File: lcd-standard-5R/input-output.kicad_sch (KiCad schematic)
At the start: 20 parts, among them J8 Serial, J9 Conn_01x10_MountingPin, Q2 MMBT3904, Q3 MMBT3904, Q4 MMBT3904, SW3 BOOT0, SW4 RST

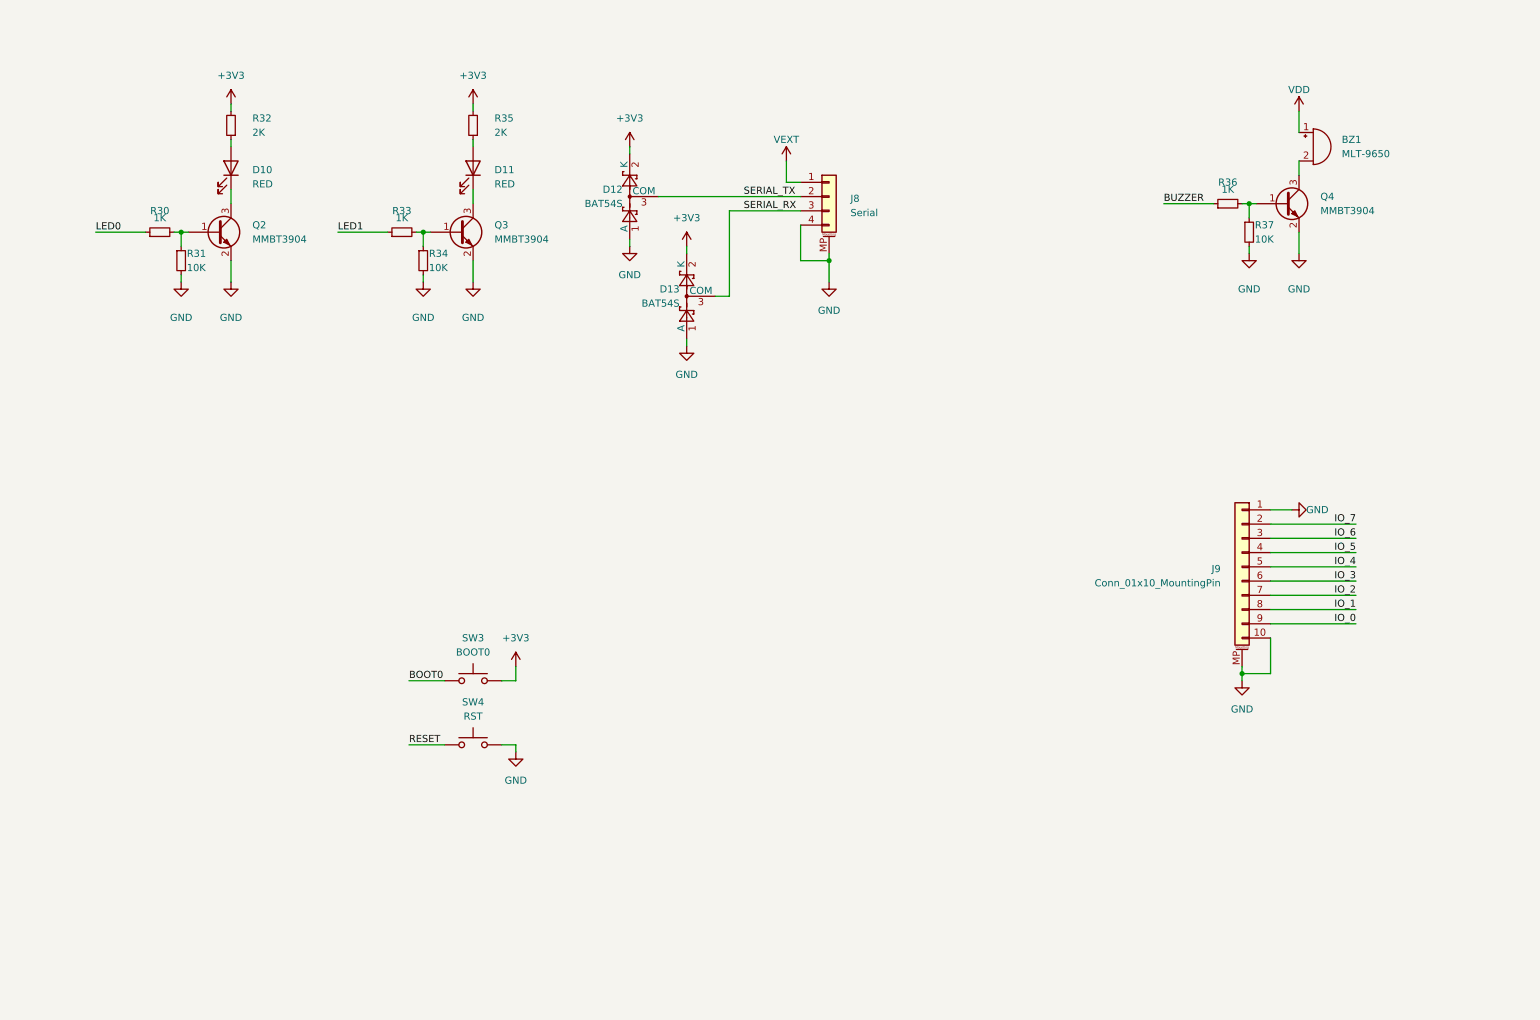
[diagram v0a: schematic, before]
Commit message: Change MCU to STM32H743
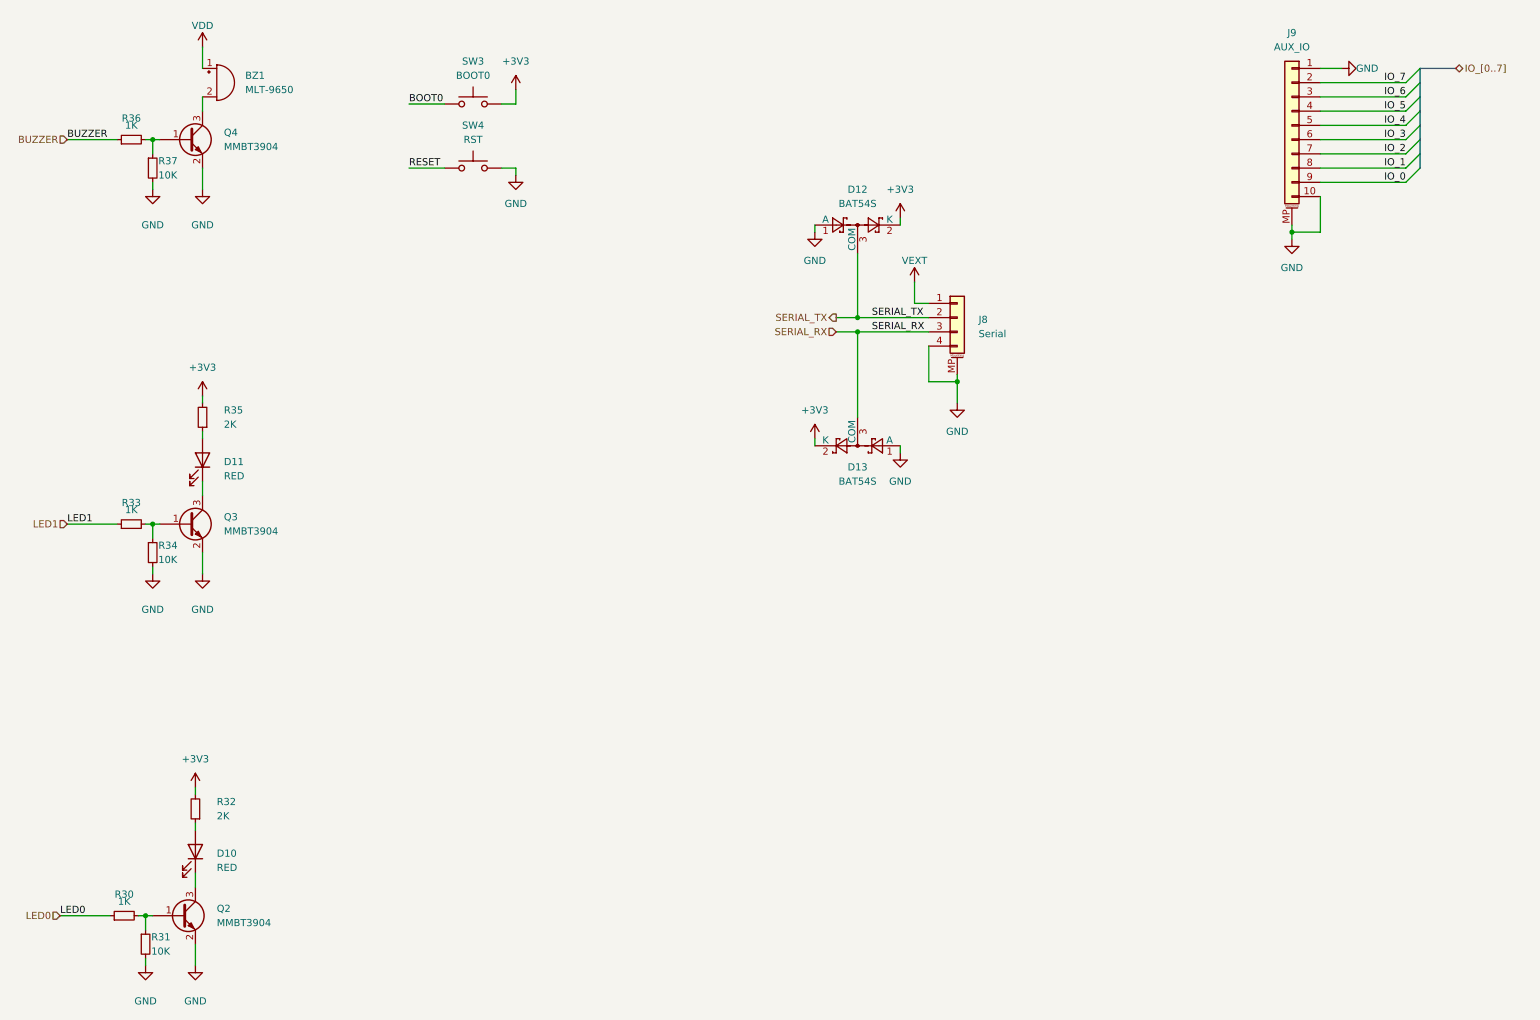
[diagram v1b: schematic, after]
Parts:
- J9: value Conn_01x10_MountingPin -> AUX_IO
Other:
- moved on the sheet: BZ1, D10, D11, D12, D13, J8, J9, Q2, Q3, Q4, R30, R31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

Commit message: Finsihed, need to touch up a bit
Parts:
- added C58, C59: 100n, Capacitor_SMD:C_0402_1005Metric, symbol Device:C_Small
- added R41, R42: 10K, Resistor_SMD:R_0402_1005Metric, symbol Device:R_Small
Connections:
- net +3V3: now also R41.1, R42.1; no longer SW3.2
- net GND: now also SW3.2, C58.2, C59.2
- net BOOT0 renamed BTN_0
- net BTN_0: now also C58.1, R41.2
- net RESET renamed BTN_1
- net BTN_1: now also C59.1, R42.2
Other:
- moved on the sheet: SW4

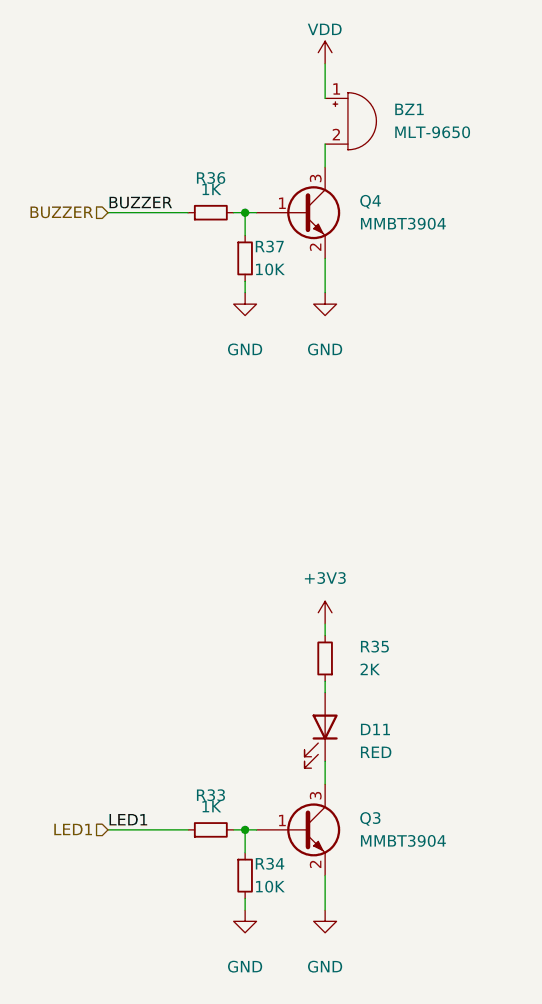
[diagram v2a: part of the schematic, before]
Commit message: Adding filter on MAX98357, TODO: Add more grounding vias
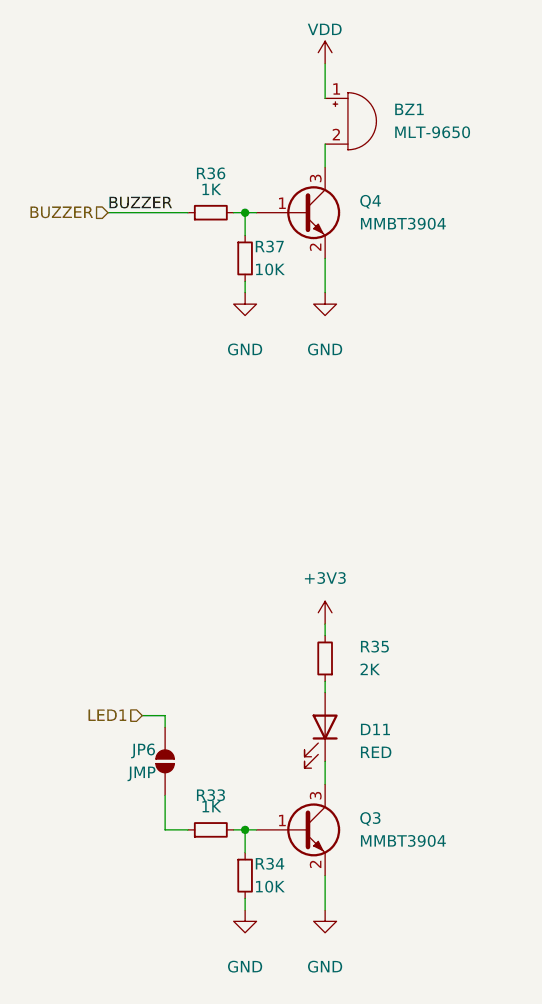
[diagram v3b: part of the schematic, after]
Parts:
- added JP6: JMP, Jumper:SolderJumper-2_P1.3mm_Open_RoundedPad1.0x1.5mm, symbol Jumper:SolderJumper_2_Open
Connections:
- net LED1: now also JP6.2 (B); no longer R33.1
- new net: JP6.1 (A), R33.1
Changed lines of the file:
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@@
 	(wire
 		(pts
+			(xy 27.94 95.25) (xy 30.48 95.25)
+		)
+		(stroke
+			(width 0)
+			(type default)
+		)
+	)
+	(wire
+		(pts
 			(xy 177.8 82.55) (xy 182.88 82.55)
 		)
@@
 	(wire
 		(pts
+			(xy 30.48 95.25) (xy 30.48 96.52)
+		)
+		(stroke
+			(width 0)
+			(type default)
+		)
+	)
+	(wire
+		(pts
 			(xy 22.86 177.8) (xy 31.75 177.8)
 		)
@@
 	(wire
 		(pts
+			(xy 30.48 107.95) (xy 33.02 107.95)
+		)
+		(stroke
+			(width 0)
+			(type default)
+		)
+	)
+	(wire
+		(pts
 			(xy 182.88 86.36) (xy 182.88 82.55)
 		)
@@
 	(wire
 		(pts
+			(xy 30.48 104.14) (xy 30.48 107.95)
+		)
+		(stroke
+			(width 0)
+			(type default)
+		)
+	)
+	(wire
+		(pts
 			(xy 242.57 55.88) (xy 242.57 54.61)
 		)
@@
 	(wire
 		(pts
-			(xy 24.13 107.95) (xy 33.02 107.95)
-		)
-		(stroke
-			(width 0)
-			(type default)
-		)
-	)
-	(wire
-		(pts
 			(xy 262.89 36.83) (xy 247.65 36.83)
 		)
@@
 		)
 	)
-	(label "LED1"
-		(at 24.13 107.95 0)
-		(fields_autoplaced yes)
-		(effects
-			(font
-				(size 1.27 1.27)
-			)
-			(justify left bottom)
-		)
-	)
 	(label "IO_7"
 		(at 262.89 29.21 180)
@@
 	(hierarchical_label "LED1"
 		(shape input)
-		(at 24.13 107.95 180)
+		(at 27.94 95.25 180)
 		(fields_autoplaced yes)
 		(effects
@@
 		(on_board yes)
 		(dnp no)
-		(fields_autoplaced yes)
 		(property "Reference" "R36"
-			(at 35.56 35.56 90)
+			(at 35.56 35.052 90)
 			(effects
 				(font
@@
 					(unit 1)
 				)
+			)
+		)
+	)
+	(symbol
+		(lib_id "Jumper:SolderJumper_2_Open")
+		(at 30.48 100.33 270)
+		(mirror x)
+		(unit 1)
+		(exclude_from_sim yes)
+		(in_bom no)
+		(on_board yes)
+		(dnp no)
+		(property "Reference" "JP6"
+			(at 29.464 99.06 90)
+			(effects
+				(font
+					(size 1.27 1.27)
+				)
+				(justify right)
+			)
+		)
+		(property "Value" "JMP"
+			(at 29.464 101.6 90)
+			(effects
+				(font
+					(size 1.27 1.27)
+				)
+				(justify right)
+			)
+		)
+		(property "Footprint" "Jumper:SolderJumper-2_P1.3mm_Open_RoundedPad1.0x1.5mm"
+			(at 30.48 100.33 0)
+			(effects
+				(font
+					(size 1.27 1.27)
+				)
+				(hide yes)
+			)
+		)
+		(property "Datasheet" "~"
+			(at 30.48 100.33 0)
+			(effects
+				(font
+					(size 1.27 1.27)
+				)
+				(hide yes)
+			)
+		)
+		(property "Description" "Solder Jumper, 2-pole, open"
+			(at 30.48 100.33 0)
+			(effects
+				(font
+					(size 1.27 1.27)
+				)
+				(hide yes)
+			)
+		)
+		(property "JLCPCB Part #" ""
+			(at 30.48 100.33 0)
+			(effects
+				(font
+					(size 1.27 1.27)
+				)
+				(hide yes)
+			)
+		)
+		(pin "1"
+		)
+		(pin "2"
+		)
+		(instances
+			(project "lcd-standard-5R"
+				(path "/a9fe5be7-3a80-455e-a721-d53819db4a52/fe784777-4ebf-46af-8dff-f54c8123e5a9"
+					(reference "JP6")
+					(unit 1)
+				)

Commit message: Add QSPI Flash trace length matching to 5 inch LCD
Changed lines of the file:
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@@
 (kicad_sch
-	(version 20231120)
+	(version 20250114)
 	(generator "eeschema")
-	(generator_version "8.0")
+	(generator_version "9.0")
 	(paper "A4")
 	(junction
@@
 	(label "IO_2"
 		(at 262.89 41.91 180)
-		(fields_autoplaced yes)
 		(effects
 			(font
@@
 	(label "LED0"
 		(at 22.86 177.8 0)
-		(fields_autoplaced yes)
 		(effects
 			(font
@@
 	(label "IO_6"
 		(at 262.89 31.75 180)
-		(fields_autoplaced yes)
 		(effects
 			(font
@@
 	(label "IO_5"
 		(at 262.89 34.29 180)
-		(fields_autoplaced yes)
 		(effects
 			(font
@@
 	(label "IO_0"
 		(at 262.89 46.99 180)
-		(fields_autoplaced yes)
 		(effects
 			(font
@@
 	(label "IO_4"
 		(at 262.89 36.83 180)
-		(fields_autoplaced yes)
 		(effects
 			(font
@@
 	(label "BUZZER"
 		(at 24.13 39.37 0)
-		(fields_autoplaced yes)
 		(effects
 			(font
@@
 	(label "IO_1"
 		(at 262.89 44.45 180)
-		(fields_autoplaced yes)
 		(effects
 			(font
@@
 	(label "SERIAL_TX"
 		(at 167.64 71.12 0)
-		(fields_autoplaced yes)
 		(effects
 			(font
@@
 	(label "IO_3"
 		(at 262.89 39.37 180)
-		(fields_autoplaced yes)
 		(effects
 			(font
@@
 	(label "IO_7"
 		(at 262.89 29.21 180)
-		(fields_autoplaced yes)
 		(effects
 			(font
@@
 	(label "SERIAL_RX"
 		(at 167.64 73.66 0)
-		(fields_autoplaced yes)
 		(effects
 			(font
@@
 		(shape input)
 		(at 161.29 73.66 180)
-		(fields_autoplaced yes)
 		(effects
 			(font
@@
 		(shape output)
 		(at 85.09 33.02 180)
-		(fields_autoplaced yes)
 		(effects
 			(font
@@
 		(shape input)
 		(at 24.13 39.37 180)
-		(fields_autoplaced yes)
 		(effects
 			(font
@@
 		(shape input)
 		(at 27.94 95.25 180)
-		(fields_autoplaced yes)
 		(effects
 			(font
@@
 		(shape bidirectional)
 		(at 271.78 26.67 0)
-		(fields_autoplaced yes)
 		(effects
 			(font
@@
 		(shape output)
 		(at 161.29 71.12 180)
-		(fields_autoplaced yes)
 		(effects
 			(font
@@
 		(shape output)
 		(at 85.09 67.31 180)
-		(fields_autoplaced yes)
 		(effects
 			(font
@@
 		(shape input)
 		(at 22.86 177.8 180)
-		(fields_autoplaced yes)
-		(effects
-			(font
+		(effects
+			(font
